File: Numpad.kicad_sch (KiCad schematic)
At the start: 106 parts, among them J1 USB_C_Receptacle_USB2.0, J3 AVR-ISP-6, Q2 DMN2041L, SW10 SW_Push, SW11 SW_Push, SW12 SW_Push, SW13 SW_Push, SW14 SW_Push, SW15 SW_Push, SW16 SW_Push, SW17 SW_Push, SW18 SW_Push, SW19 SW_Push, SW2 SW_Push, SW21 SW_Push, SW3 SW_Push, SW4 SW_Push, SW5 SW_Push, SW6 SW_Push, SW7 SW_Push, SW8 SW_Push, SW9 SW_Push, U1 ATmega32U2-A, Y1 16MHz

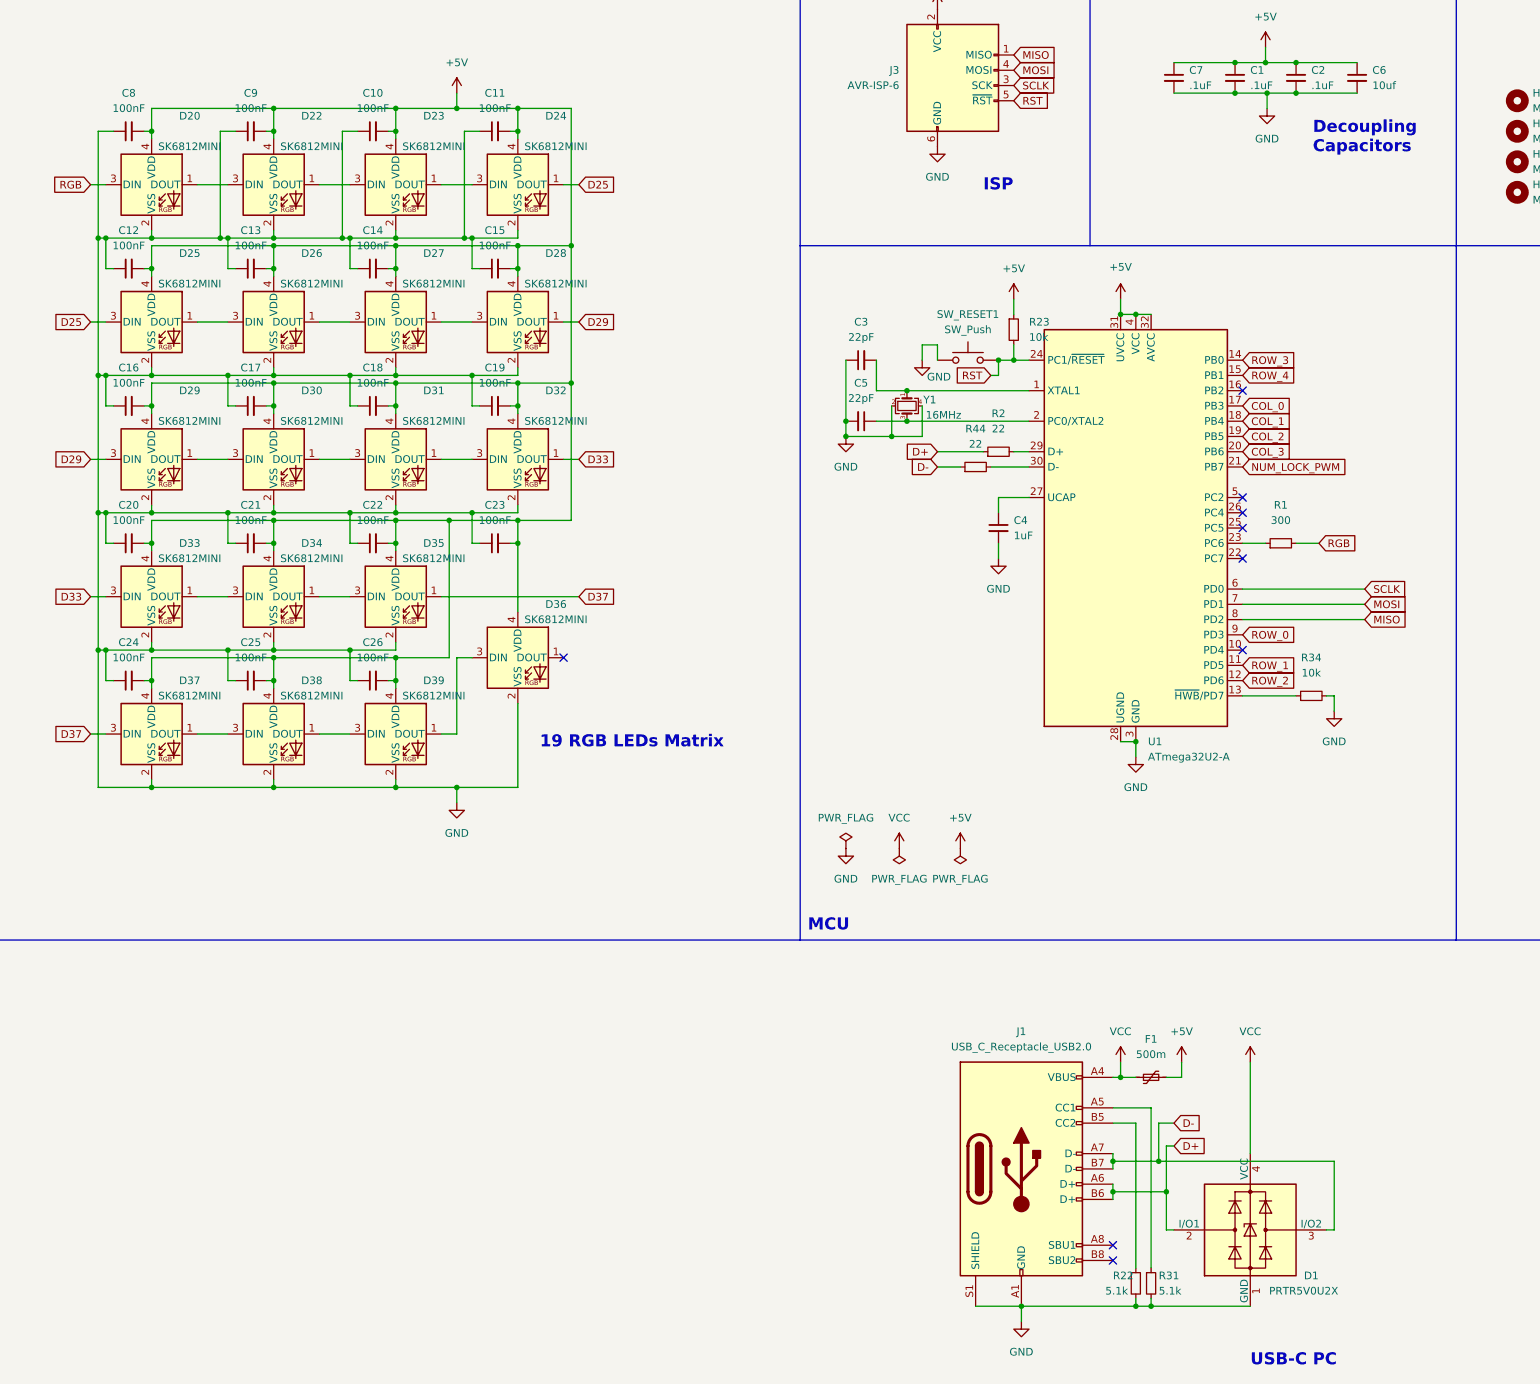
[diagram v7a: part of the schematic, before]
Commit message: did a lot of work on the numpad, basically it's "finished"
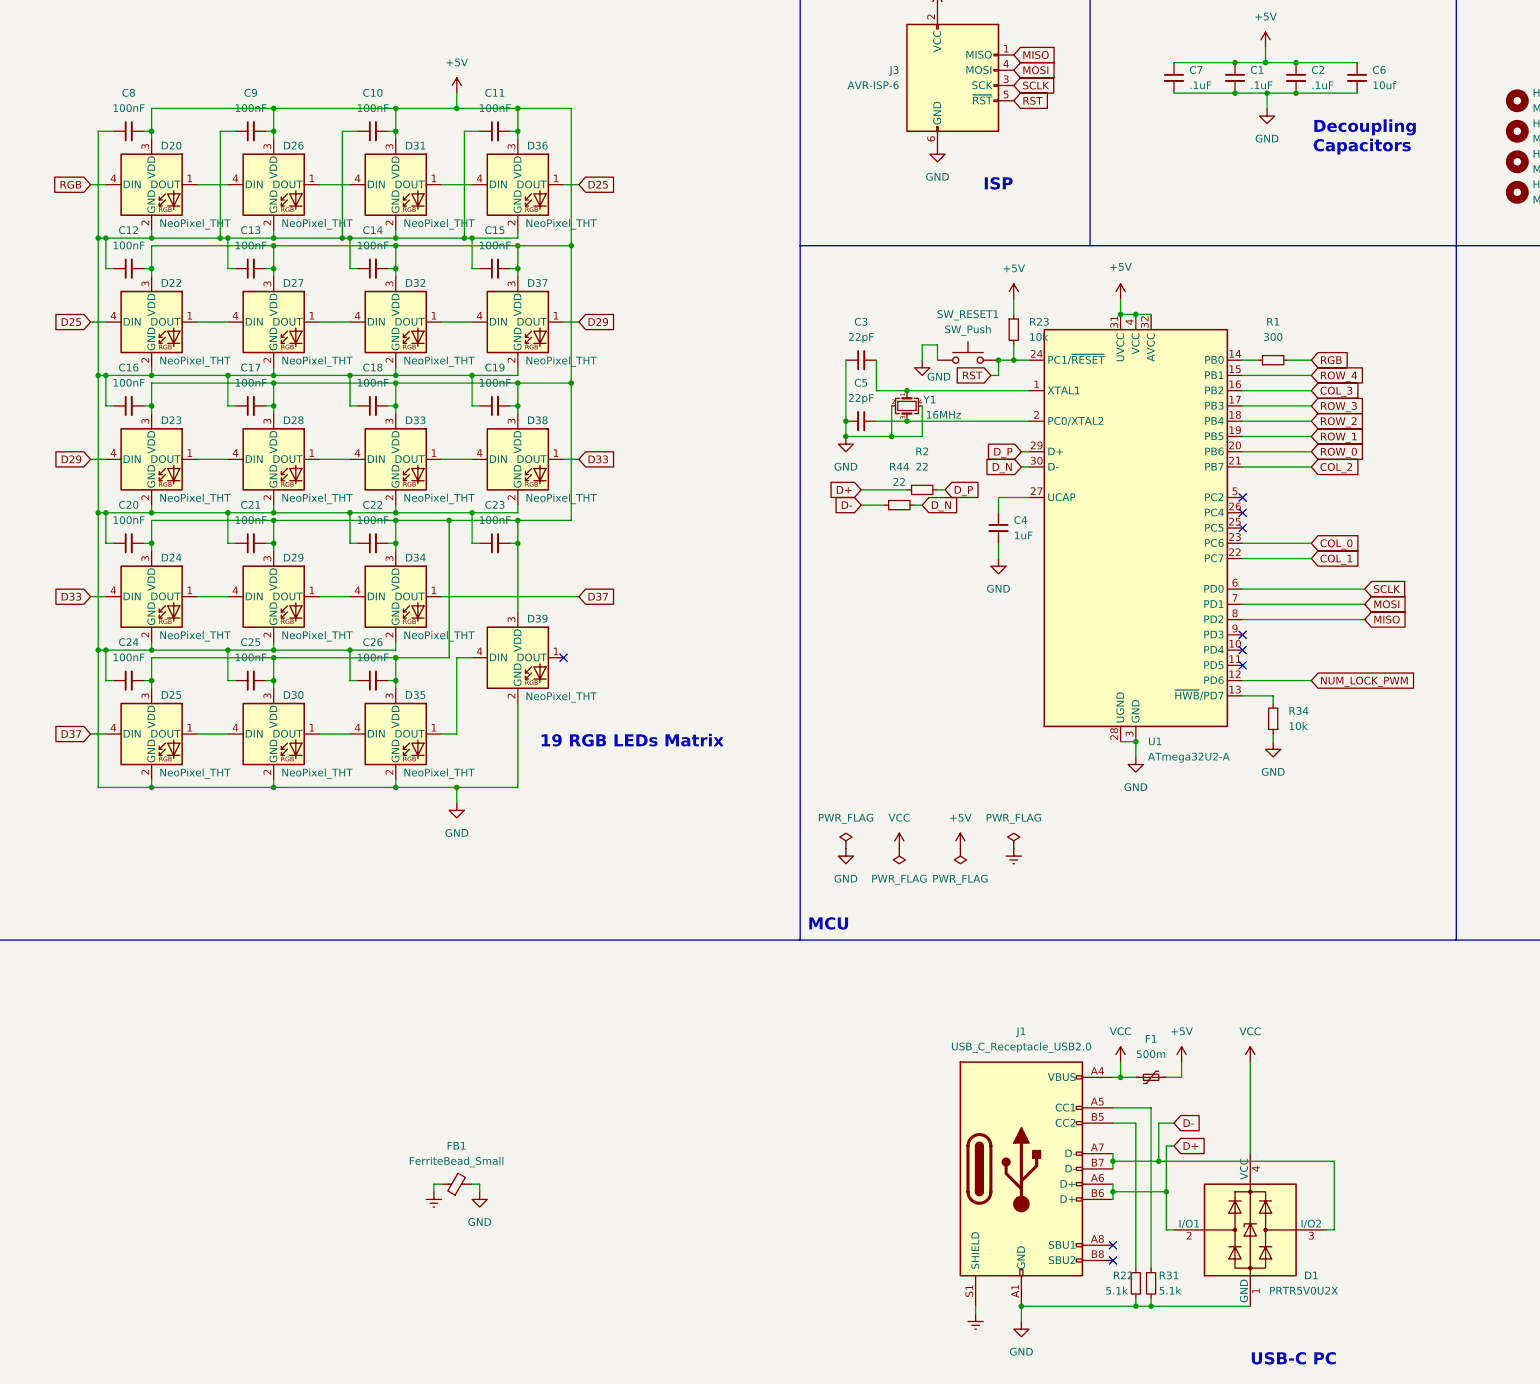
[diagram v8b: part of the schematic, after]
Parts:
- added FB1: FerriteBead_Small, Inductor_SMD:L_0805_2012Metric_Pad1.15x1.40mm_HandSolder, symbol Device:FerriteBead_Small
- D20: value SK6812MINI -> NeoPixel_THT; footprint Keebio-Parts:SK6812-MINI-E -> kicad-keyboard-parts.pretty:LED_RGB_Wuerth-PLCC4_3.2x2.8mm_150141M173100; symbol LED:SK6812MINI -> LED:NeoPixel_THT
- D22: renamed from D25; value SK6812MINI -> NeoPixel_THT; footprint Keebio-Parts:SK6812-MINI-E -> kicad-keyboard-parts.pretty:LED_RGB_Wuerth-PLCC4_3.2x2.8mm_150141M173100; symbol LED:SK6812MINI -> LED:NeoPixel_THT
- D23: renamed from D29; value SK6812MINI -> NeoPixel_THT; footprint Keebio-Parts:SK6812-MINI-E -> kicad-keyboard-parts.pretty:LED_RGB_Wuerth-PLCC4_3.2x2.8mm_150141M173100; symbol LED:SK6812MINI -> LED:NeoPixel_THT
- D24: renamed from D33; value SK6812MINI -> NeoPixel_THT; footprint Keebio-Parts:SK6812-MINI-E -> kicad-keyboard-parts.pretty:LED_RGB_Wuerth-PLCC4_3.2x2.8mm_150141M173100; symbol LED:SK6812MINI -> LED:NeoPixel_THT
- D25: renamed from D37; value SK6812MINI -> NeoPixel_THT; footprint Keebio-Parts:SK6812-MINI-E -> kicad-keyboard-parts.pretty:LED_RGB_Wuerth-PLCC4_3.2x2.8mm_150141M173100; symbol LED:SK6812MINI -> LED:NeoPixel_THT
- D26: renamed from D22; value SK6812MINI -> NeoPixel_THT; footprint Keebio-Parts:SK6812-MINI-E -> kicad-keyboard-parts.pretty:LED_RGB_Wuerth-PLCC4_3.2x2.8mm_150141M173100; symbol LED:SK6812MINI -> LED:NeoPixel_THT
- D27: renamed from D26; value SK6812MINI -> NeoPixel_THT; footprint Keebio-Parts:SK6812-MINI-E -> kicad-keyboard-parts.pretty:LED_RGB_Wuerth-PLCC4_3.2x2.8mm_150141M173100; symbol LED:SK6812MINI -> LED:NeoPixel_THT
- D28: renamed from D30; value SK6812MINI -> NeoPixel_THT; footprint Keebio-Parts:SK6812-MINI-E -> kicad-keyboard-parts.pretty:LED_RGB_Wuerth-PLCC4_3.2x2.8mm_150141M173100; symbol LED:SK6812MINI -> LED:NeoPixel_THT
- D29: renamed from D34; value SK6812MINI -> NeoPixel_THT; footprint Keebio-Parts:SK6812-MINI-E -> kicad-keyboard-parts.pretty:LED_RGB_Wuerth-PLCC4_3.2x2.8mm_150141M173100; symbol LED:SK6812MINI -> LED:NeoPixel_THT
- D30: renamed from D38; value SK6812MINI -> NeoPixel_THT; footprint Keebio-Parts:SK6812-MINI-E -> kicad-keyboard-parts.pretty:LED_RGB_Wuerth-PLCC4_3.2x2.8mm_150141M173100; symbol LED:SK6812MINI -> LED:NeoPixel_THT
- D31: renamed from D23; value SK6812MINI -> NeoPixel_THT; footprint Keebio-Parts:SK6812-MINI-E -> kicad-keyboard-parts.pretty:LED_RGB_Wuerth-PLCC4_3.2x2.8mm_150141M173100; symbol LED:SK6812MINI -> LED:NeoPixel_THT
- D32: renamed from D27; value SK6812MINI -> NeoPixel_THT; footprint Keebio-Parts:SK6812-MINI-E -> kicad-keyboard-parts.pretty:LED_RGB_Wuerth-PLCC4_3.2x2.8mm_150141M173100; symbol LED:SK6812MINI -> LED:NeoPixel_THT
- D33: renamed from D31; value SK6812MINI -> NeoPixel_THT; footprint Keebio-Parts:SK6812-MINI-E -> kicad-keyboard-parts.pretty:LED_RGB_Wuerth-PLCC4_3.2x2.8mm_150141M173100; symbol LED:SK6812MINI -> LED:NeoPixel_THT
- D34: renamed from D35; value SK6812MINI -> NeoPixel_THT; footprint Keebio-Parts:SK6812-MINI-E -> kicad-keyboard-parts.pretty:LED_RGB_Wuerth-PLCC4_3.2x2.8mm_150141M173100; symbol LED:SK6812MINI -> LED:NeoPixel_THT
- D35: renamed from D39; value SK6812MINI -> NeoPixel_THT; footprint Keebio-Parts:SK6812-MINI-E -> kicad-keyboard-parts.pretty:LED_RGB_Wuerth-PLCC4_3.2x2.8mm_150141M173100; symbol LED:SK6812MINI -> LED:NeoPixel_THT
- D36: renamed from D24; value SK6812MINI -> NeoPixel_THT; footprint Keebio-Parts:SK6812-MINI-E -> kicad-keyboard-parts.pretty:LED_RGB_Wuerth-PLCC4_3.2x2.8mm_150141M173100; symbol LED:SK6812MINI -> LED:NeoPixel_THT
- D37: renamed from D28; value SK6812MINI -> NeoPixel_THT; footprint Keebio-Parts:SK6812-MINI-E -> kicad-keyboard-parts.pretty:LED_RGB_Wuerth-PLCC4_3.2x2.8mm_150141M173100; symbol LED:SK6812MINI -> LED:NeoPixel_THT
- D38: renamed from D32; value SK6812MINI -> NeoPixel_THT; footprint Keebio-Parts:SK6812-MINI-E -> kicad-keyboard-parts.pretty:LED_RGB_Wuerth-PLCC4_3.2x2.8mm_150141M173100; symbol LED:SK6812MINI -> LED:NeoPixel_THT
- D39: renamed from D36; value SK6812MINI -> NeoPixel_THT; footprint Keebio-Parts:SK6812-MINI-E -> kicad-keyboard-parts.pretty:LED_RGB_Wuerth-PLCC4_3.2x2.8mm_150141M173100; symbol LED:SK6812MINI -> LED:NeoPixel_THT
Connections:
- net +5V: now also D20.3 (VDD), D22.3 (VDD), D23.3 (VDD), D24.3 (VDD), D25.3 (VDD), D26.3 (VDD), D27.3 (VDD), D28.3 (VDD), D29.3 (VDD), D30.3 (VDD), D31.3 (VDD), D32.3 (VDD), D33.3 (VDD), D34.3 (VDD), D35.3 (VDD), D36.3 (VDD), D37.3 (VDD), D38.3 (VDD), D39.3 (VDD); no longer D20.4 (VDD), D22.4 (VDD), D23.4 (VDD), D24.4 (VDD), D25.4 (VDD), D26.4 (VDD), D27.4 (VDD), D28.4 (VDD), D29.4 (VDD), D30.4 (VDD), D31.4 (VDD), D32.4 (VDD), D33.4 (VDD), D34.4 (VDD), D35.4 (VDD), D36.4 (VDD), D37.4 (VDD), D38.4 (VDD), D39.4 (VDD)
- net COL_0: now also U1.23 (PC6); no longer U1.17 (PB3)
- net COL_1: now also U1.22 (PC7); no longer U1.18 (PB4)
- net COL_2: now also U1.21 (PB7); no longer U1.19 (PB5)
- net COL_3: now also U1.16 (PB2); no longer U1.20 (PB6)
- net D25: now also D22.4 (DIN); no longer D22.3 (DIN)
- net D29: now also D23.4 (DIN); no longer D23.3 (DIN)
- net D33: now also D24.4 (DIN); no longer D24.3 (DIN)
- net D37: now also D25.4 (DIN); no longer D25.3 (DIN)
- net GND: now also R34.1, FB1.2; no longer J1.S1 (SHIELD), R34.2
- net NUM_LOCK_PWM: now also U1.12 (PD6); no longer U1.21 (PB7)
- net RGB: now also D20.4 (DIN); no longer D20.3 (DIN)
- net ROW_0: now also U1.20 (PB6); no longer U1.9 (PD3)
- net ROW_1: now also U1.19 (PB5); no longer U1.11 (PD5)
- net ROW_2: now also U1.18 (PB4); no longer U1.12 (PD6)
- net ROW_3: now also U1.17 (PB3); no longer U1.14 (PB0)
- net D_P: now reaches R2.2, U1.29 (D+)
- net at D22.1 (DOUT): now also D27.4 (DIN); no longer D27.3 (DIN)
- net at D31.1 (DOUT): now also D36.4 (DIN); no longer D36.3 (DIN)
- net at D26.1 (DOUT): now also D31.4 (DIN); no longer D31.3 (DIN)
- net at D33.1 (DOUT): now also D38.4 (DIN); no longer D38.3 (DIN)
- net at D35.1 (DOUT): now also D39.4 (DIN); no longer D39.3 (DIN)
- net at D30.1 (DOUT): now also D35.4 (DIN); no longer D35.3 (DIN)
- net at D28.1 (DOUT): now also D33.4 (DIN); no longer D33.3 (DIN)
- net at D23.1 (DOUT): now also D28.4 (DIN); no longer D28.3 (DIN)
- net at D20.1 (DOUT): now also D26.4 (DIN); no longer D26.3 (DIN)
- net at D29.1 (DOUT): now also D34.4 (DIN); no longer D34.3 (DIN)
- net at D24.1 (DOUT): now also D29.4 (DIN); no longer D29.3 (DIN)
- net at D32.1 (DOUT): now also D37.4 (DIN); no longer D37.3 (DIN)
- net at D27.1 (DOUT): now also D32.4 (DIN); no longer D32.3 (DIN)
- net at R1.1: now also U1.14 (PB0); no longer U1.23 (PC6)
- net at U1.13 (~{HWB}/PD7): now also R34.2; no longer R34.1
- net D_N: now reaches R44.2, U1.30 (D-)
- net at D25.1 (DOUT): now also D30.4 (DIN); no longer D30.3 (DIN)
- new net Earth: FB1.1, J1.S1 (SHIELD)
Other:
- moved on the sheet: R1, R2, R34, R44
